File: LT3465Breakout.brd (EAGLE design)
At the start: 50 x 72.7 mm, 39 parts

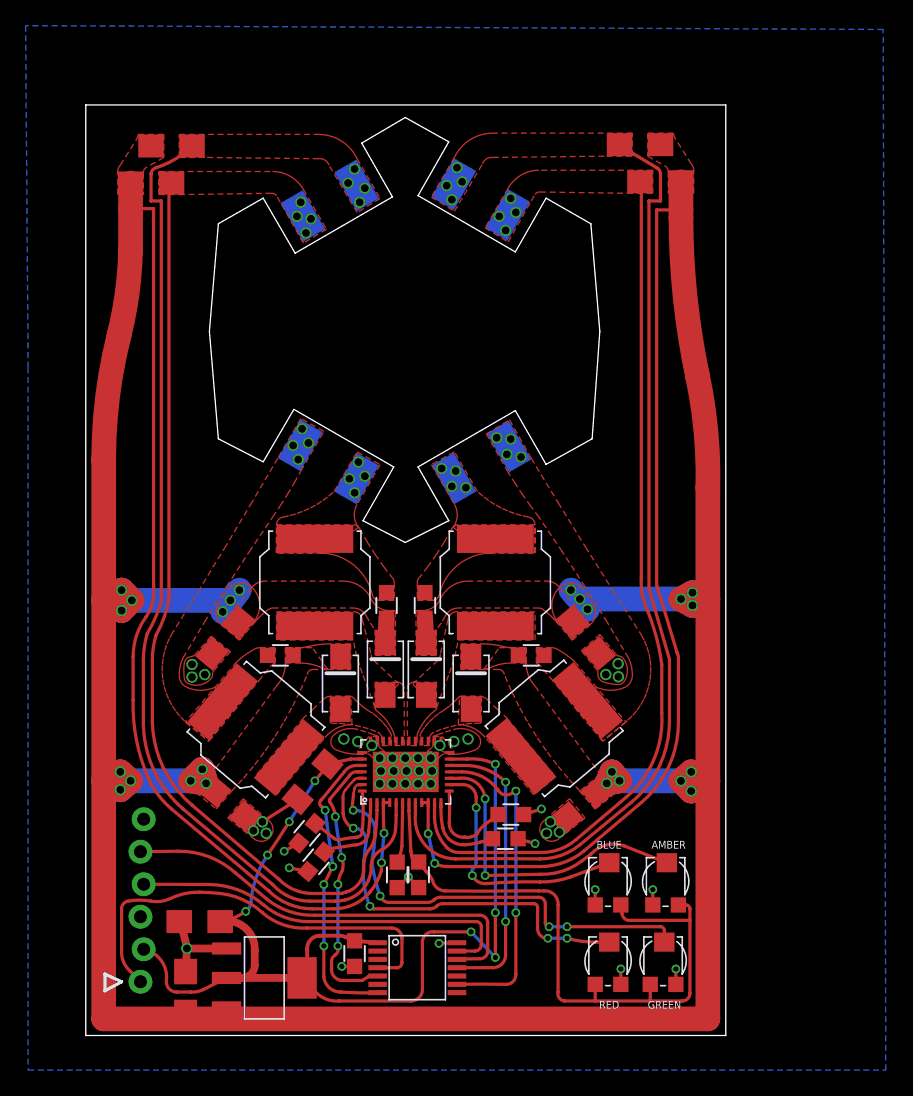
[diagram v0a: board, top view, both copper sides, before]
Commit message: Added comm header, general cleanup, more labels.
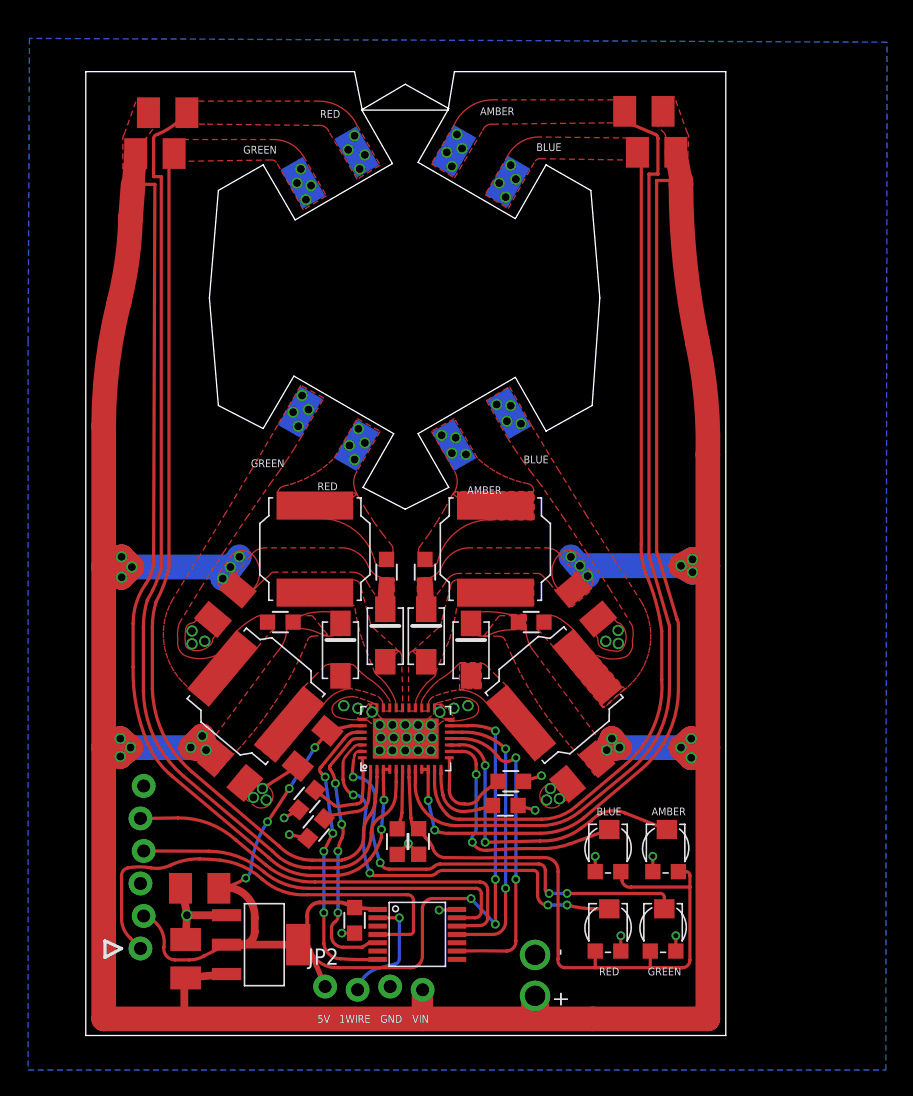
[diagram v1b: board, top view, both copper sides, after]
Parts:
- added JP2: (no value), 1dah:1X04_LOCK
- added U$17: POWER_SOLDER-1.5, 1dah:POWER_SOLDER
- moved R3 2.62 mm to (6.40, 72.1)
- moved R4 2.62 mm to (43.6, 72.2)
- moved C1 2.60 mm to (17.7, 22.4)
- moved C11 2.60 mm to (11.3, 20.7)
- moved C12 2.60 mm to (10.9, 33.7)
- moved C14 2.60 mm to (38.8, 20.6)
- moved C6 2.60 mm to (33.2, 19.9)
- moved C7 2.60 mm to (15.2, 32.3)
- moved C8 2.60 mm to (23.5, 36.2)
- moved C9 2.60 mm to (26.5, 36.2)
- moved JP1 2.60 mm to (4.40, 19.5)
- moved U$10 2.60 mm to (36.6, 26.6)
- moved U$4 2.60 mm to (23.4, 31.2)
- moved U$6 2.60 mm to (30.1, 30.1)
- moved U$7 2.60 mm to (13.3, 26.5)
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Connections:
- new net N$1: U$2.3
- new net N$2: JP2.2, U$2.2
- net 5V: now also JP2.1
- net GND: now also JP2.3, U$17.-
- net VIN: now also JP2.4, U$17.+
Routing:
- net VIN: track 417.9 -> 435.1 mm
- net N$2: track 0.00 -> 9.10 mm, vias 0 -> 1
- net 5V: track 88.0 -> 91.4 mm
- net MCLR: track 33.2 -> 35.3 mm
- net LED2: track 79.9 -> 79.3 mm
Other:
- board size 50 x 72.7 mm -> 50 x 75.3 mm
- board text added: "1WIRE"
- board text added: "5V"
- board text added: "GND"
- board text added: "VIN"
